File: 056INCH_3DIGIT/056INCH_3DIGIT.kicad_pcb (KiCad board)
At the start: 2 copper layers, 43.8 x 21 mm, 2 parts, among them U1 BA56-12SRWA, U2 TM1637

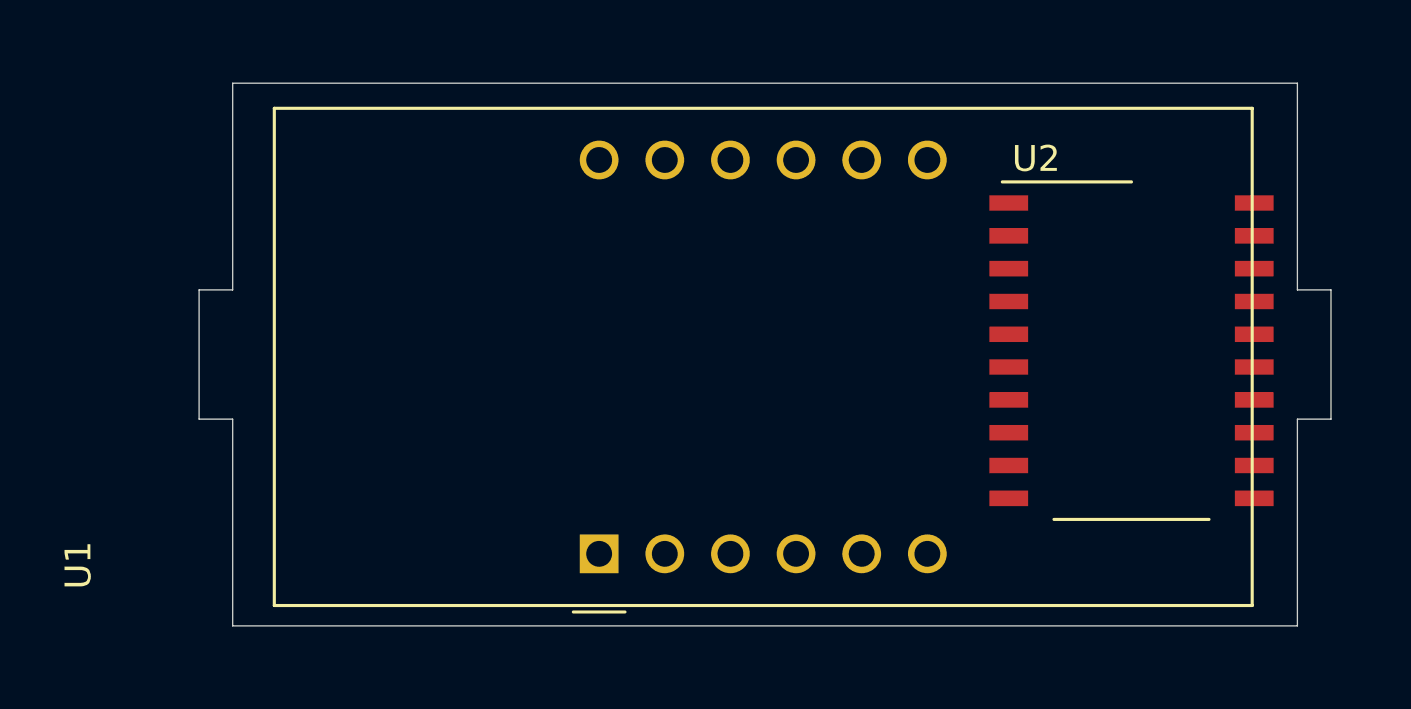
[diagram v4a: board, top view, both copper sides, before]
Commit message: all traces routed
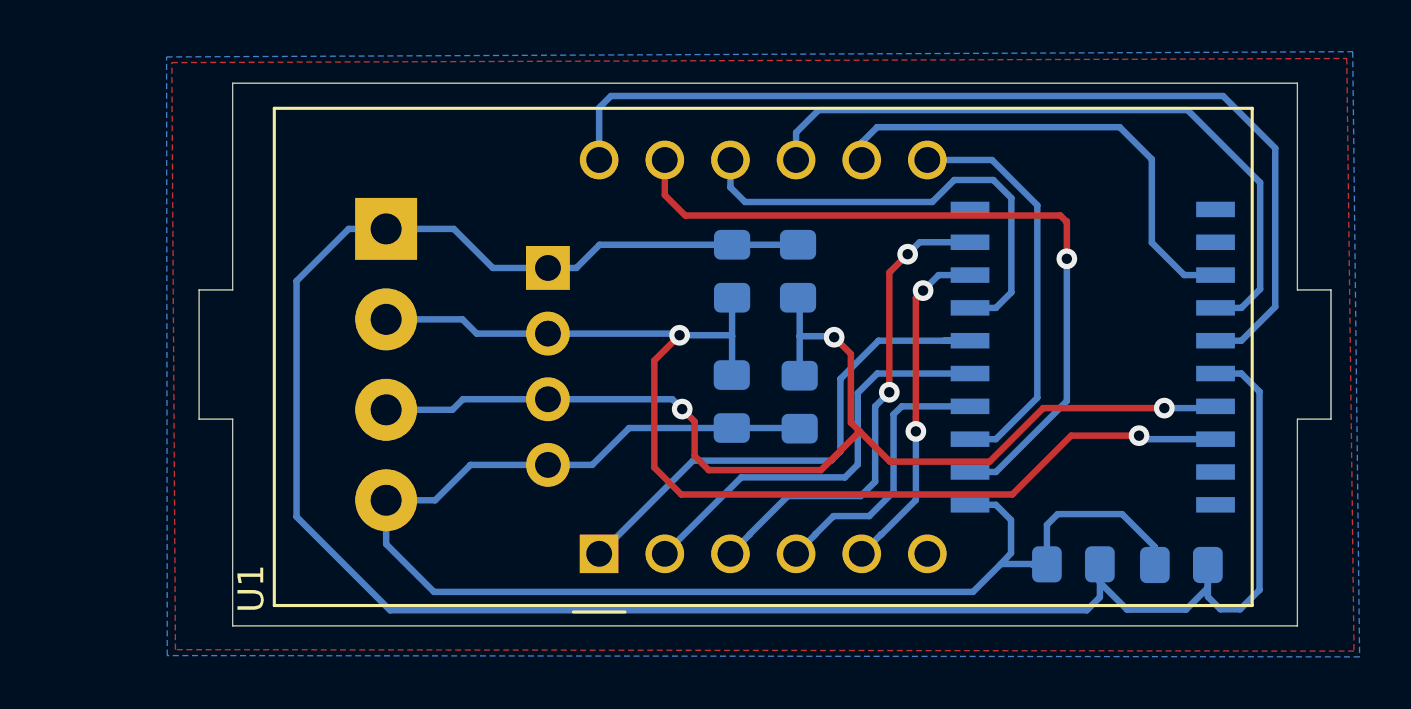
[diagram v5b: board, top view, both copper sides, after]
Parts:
- added C1: 10uF, Capacitor_SMD:C_0805_2012Metric_Pad1.15x1.40mm_HandSolder, B.Cu at (138.0, 118.6)
- added C2: 100nF, Capacitor_SMD:C_0805_2012Metric_Pad1.15x1.40mm_HandSolder, B.Cu at (133.8, 118.6)
- added C3: 100pF, Capacitor_SMD:C_0805_2012Metric_Pad1.15x1.40mm_HandSolder, B.Cu at (120.6, 112.3)
- added C4: 100pF, Capacitor_SMD:C_0805_2012Metric_Pad1.15x1.40mm_HandSolder, B.Cu at (123.2, 112.3)
- added J1: Conn_01x04_Female, TerminalBlock_4Ucon:TerminalBlock_4Ucon_1x04_P3.50mm_Horizontal, B.Cu at (107.2, 105.6)
- added J2: Conn_01x04_Male, Connector_PinHeader_2.54mm:PinHeader_1x04_P2.54mm_Vertical, B.Cu at (113.5, 107.1)
- added R1: 10k, Resistor_SMD:R_0805_2012Metric_Pad1.15x1.40mm_HandSolder, B.Cu at (120.6, 107.3)
- added R2: 10k, Resistor_SMD:R_0805_2012Metric_Pad1.15x1.40mm_HandSolder, B.Cu at (123.2, 107.3)
- U2: moved to B.Cu
- moved U2 1.52 mm to (134.6, 110.6)
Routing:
- net Net-(C1-Pad1): track 0.00 -> 84.4 mm
- net Net-(C1-Pad2): track 0.00 -> 56.4 mm
- net Net-(C3-Pad1): track 0.00 -> 45.3 mm, vias 0 -> 2
- net Net-(C4-Pad1): track 0.00 -> 44.6 mm, vias 0 -> 3
- net Net-(U1-Pad12): track 0.00 -> 38.2 mm
- net Net-(U1-Pad11): track 0.00 -> 29.2 mm, vias 0 -> 1
- net Net-(U1-Pad9): track 0.00 -> 26.7 mm
- net Net-(U1-Pad1): track 0.00 -> 20.4 mm
- net Net-(U1-Pad8): track 0.00 -> 18.9 mm
- net Net-(U1-Pad3): track 0.00 -> 18.7 mm, vias 0 -> 2
- net Net-(U1-Pad10): track 0.00 -> 18.3 mm
- net Net-(U1-Pad2): track 0.00 -> 16.3 mm
- net Net-(U1-Pad7): track 0.00 -> 15.7 mm
- net Net-(U1-Pad5): track 0.00 -> 13.2 mm, vias 0 -> 2
- net Net-(U1-Pad4): track 0.00 -> 10.9 mm
- added copper zone on B.Cu, net Net-(C1-Pad2)
- added copper zone on F.Cu, net Net-(C1-Pad2)
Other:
- board text added: "+ C D -"
- board text added: "056_3DIG"
